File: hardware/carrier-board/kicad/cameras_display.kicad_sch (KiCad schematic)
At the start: 0 parts

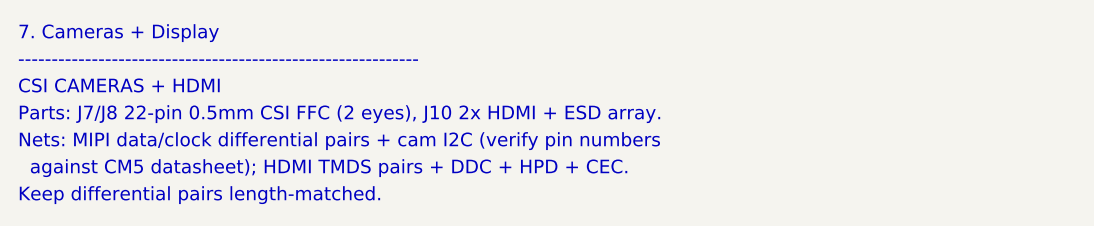
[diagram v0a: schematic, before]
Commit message: Carrier docs + KiCad plan: full two-brain pass (CM5 HUB75 + RP2354B I/O)
Propagate the two-brain architecture across the whole doc set and KiCad plan:
- REQUIREMENTS: restructured M1-M12 (CM5 HUB75; RP2354B core/MAX7219/WS2812/
  sensors/buttons/servos; USB selector + standalone program port); N-list reworked.
- POWER: add +V_SERVO and +3V3_RP rails, servo current budget, updated worked
  total + protection; sensors now on +3V3_RP not CM5 3V3.
- CONNECTORS: J3 re-sourced to RP2354B SPI0, J4 4 WS2812 zones, J5 +SENS_INT,
  J6 BTN1..10, add J12 USB-C, J20-J27 servos, SW1 USB selector, SWD/UART hdrs;
  drop JP1/JP2; fans presented as RP2354B-default-or-CM5 (decision flagged).
- BOM: add RP2354B core, '125/'245 (RP side), USB mux/USB-C/ESD, servo headers,
  +3V3_RP reg; fix '125 double-count and stale HUB75/MAX7219-shared-buffer/JP1.
- MULTI-BACKEND: HUB75+MAX7219 now simultaneous (different brains); firmware
  CompositePanelOutput is the sole remaining blocker.
- IO-EXPANSION: RP2354B is the primary I/O backbone; I2C expanders secondary.
- kicad: 11-sheet plan, stable UUIDs, generator skips populated face_buffer.
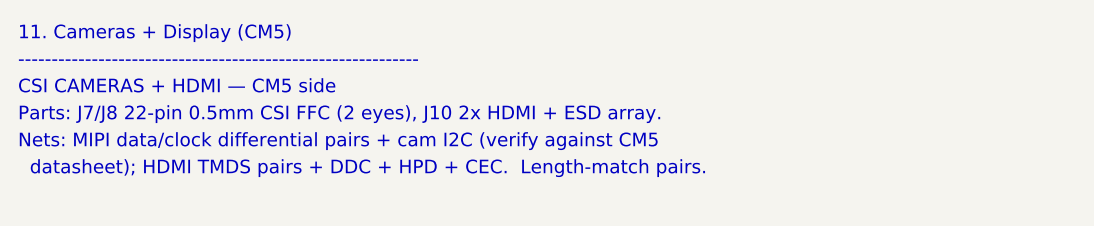
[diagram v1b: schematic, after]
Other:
- note added: "11. Cameras + Display (CM5)"
- note added: "CSI CAMERAS + HDMI — CM5 side"
- note added: "Nets: MIPI data/clock differential pairs + cam I2C (verify against CM5"
- note added: "datasheet); HDMI TMDS pairs + DDC + HPD + CEC. Length-match pairs."
- note removed: "7. Cameras + Display"
- note removed: "CSI CAMERAS + HDMI"
- note removed: "Keep differential pairs length-matched."
- note removed: "Nets: MIPI data/clock differential pairs + cam I2C (verify pin numbers"
- note removed: "against CM5 datasheet); HDMI TMDS pairs + DDC + HPD + CEC."
- title: ProtoHUD Carrier — 7. Cameras + Display -> ProtoHUD Carrier — 11. Cameras + Display (CM5)
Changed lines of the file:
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@@
   (paper "A3")
   (title_block
-    (title "ProtoHUD Carrier — 7. Cameras + Display")
+    (title "ProtoHUD Carrier — 11. Cameras + Display (CM5)")
     (rev "A")
     (company "ProtoHUD")
   )
-  (text "7. Cameras + Display" (at 25.4 25.40 0) (effects (font (size 1.5 1.5)) (justify left bottom)))
+  (text "11. Cameras + Display (CM5)" (at 25.4 25.40 0) (effects (font (size 1.5 1.5)) (justify left bottom)))
   (text "------------------------------------------------------------" (at 25.4 28.40 0) (effects (font (size 1.5 1.5)) (justify left bottom)))
-  (text "CSI CAMERAS + HDMI" (at 25.4 31.40 0) (effects (font (size 1.5 1.5)) (justify left bottom)))
+  (text "CSI CAMERAS + HDMI — CM5 side" (at 25.4 31.40 0) (effects (font (size 1.5 1.5)) (justify left bottom)))
   (text "Parts: J7/J8 22-pin 0.5mm CSI FFC (2 eyes), J10 2x HDMI + ESD array." (at 25.4 34.40 0) (effects (font (size 1.5 1.5)) (justify left bottom)))
-  (text "Nets: MIPI data/clock differential pairs + cam I2C (verify pin numbers" (at 25.4 37.40 0) (effects (font (size 1.5 1.5)) (justify left bottom)))
-  (text "  against CM5 datasheet); HDMI TMDS pairs + DDC + HPD + CEC." (at 25.4 40.40 0) (effects (font (size 1.5 1.5)) (justify left bottom)))
-  (text "Keep differential pairs length-matched." (at 25.4 43.40 0) (effects (font (size 1.5 1.5)) (justify left bottom)))
+  (text "Nets: MIPI data/clock differential pairs + cam I2C (verify against CM5" (at 25.4 37.40 0) (effects (font (size 1.5 1.5)) (justify left bottom)))
+  (text "  datasheet); HDMI TMDS pairs + DDC + HPD + CEC.  Length-match pairs." (at 25.4 40.40 0) (effects (font (size 1.5 1.5)) (justify left bottom)))
   (sheet_instances
     (path "/" (page "1"))

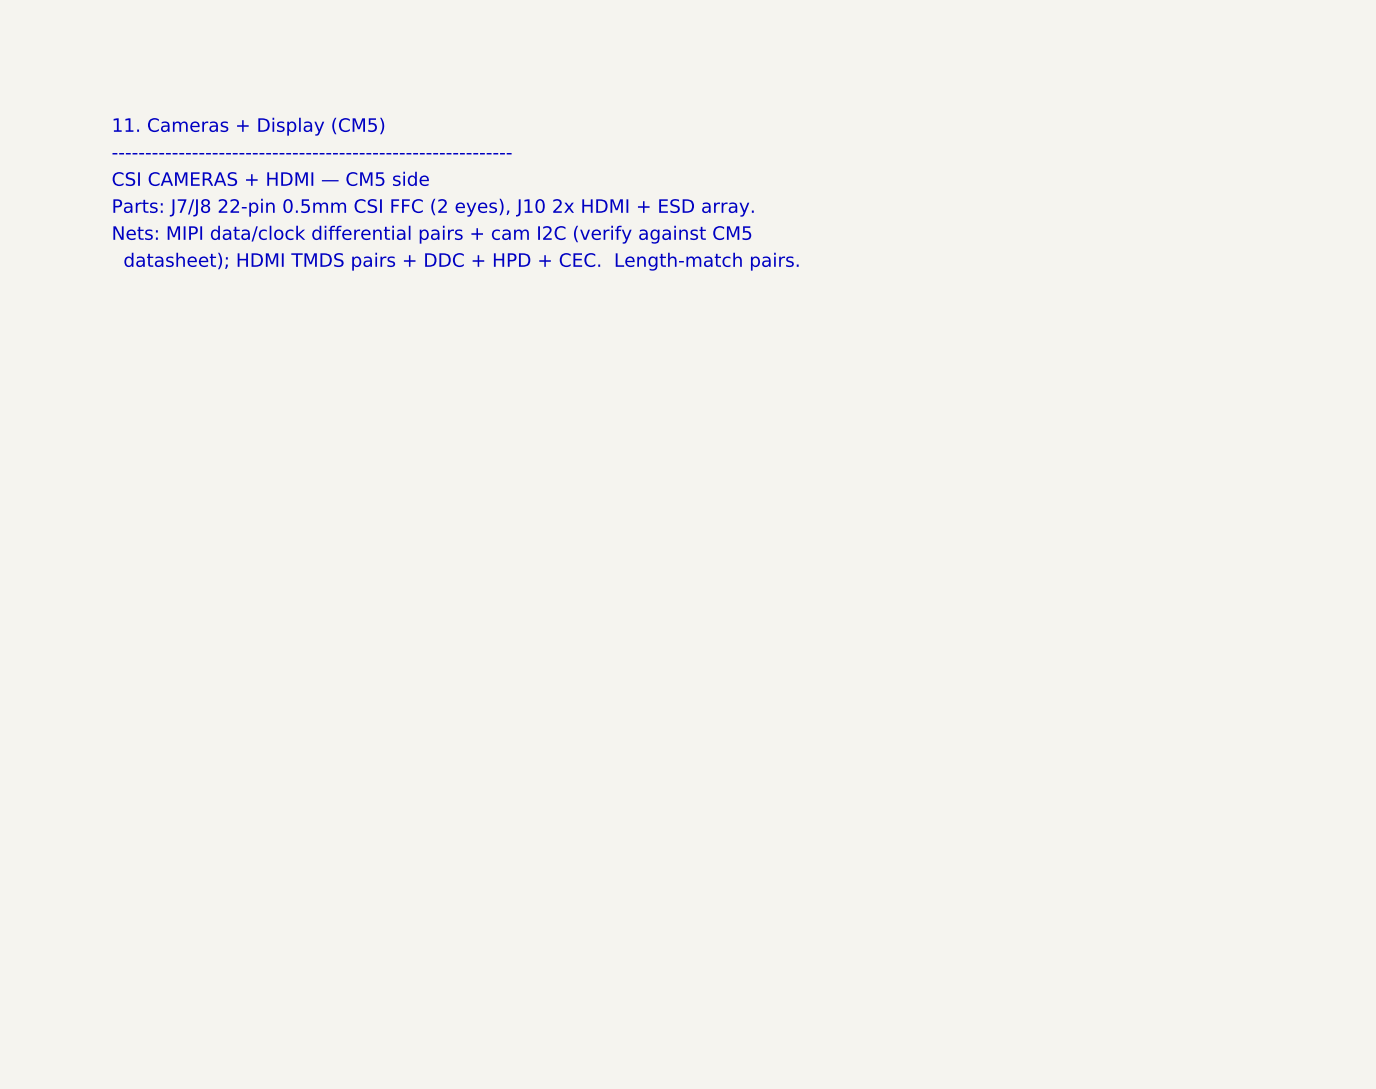
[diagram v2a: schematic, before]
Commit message: Carrier KiCad: populate all 11 schematic sheets
Replace populate_face_buffer.py with populate_sheets.py: one generator that
emits all 11 populated sub-sheets reusing the KiCad-9 format proven by the
face_buffer proof. Shared symbol library + generic box-symbol builder; condensed
CM5 (2x DF40-100) and RP2354B (QFN-80) symbols showing only used pins.

Connectivity by net labels (global for rails + cross-sheet nets: GPIOxx HUB75,
MX_*, LED*_DAT, SRV*, BTN*, *_USB_*; local within-sheet). Sheets: power
(protection + rails + AP2112 +3V3_RP), cm5 (HUB75 out + fan MOSFETs + RP ctrl),
face_buffer, rp2354_io (RP2354B + xtal + SW1/J12 + ESD + SWD), rp2354_face
(U10->J3), leds (U11 quad ->J4a-d), sensors_i2c (pull-ups+J5+STEMMA),
servos (J20-27 + rail), gpio_buttons (J6), usb (USB2514B hub + uplink),
cameras_display (CSI FFC + HDMI).

Verified: all sheets paren-balanced, every used lib_id defined, all instance
paths match sheet UUIDs, root<->sub-sheet UUID linkage intact. generate_skeleton.py
now lists all sheets POPULATED (writes only root+project). Not yet opened in
KiCad here -- expect ERC warnings (PWR_FLAG, unconnected pins) to clean.
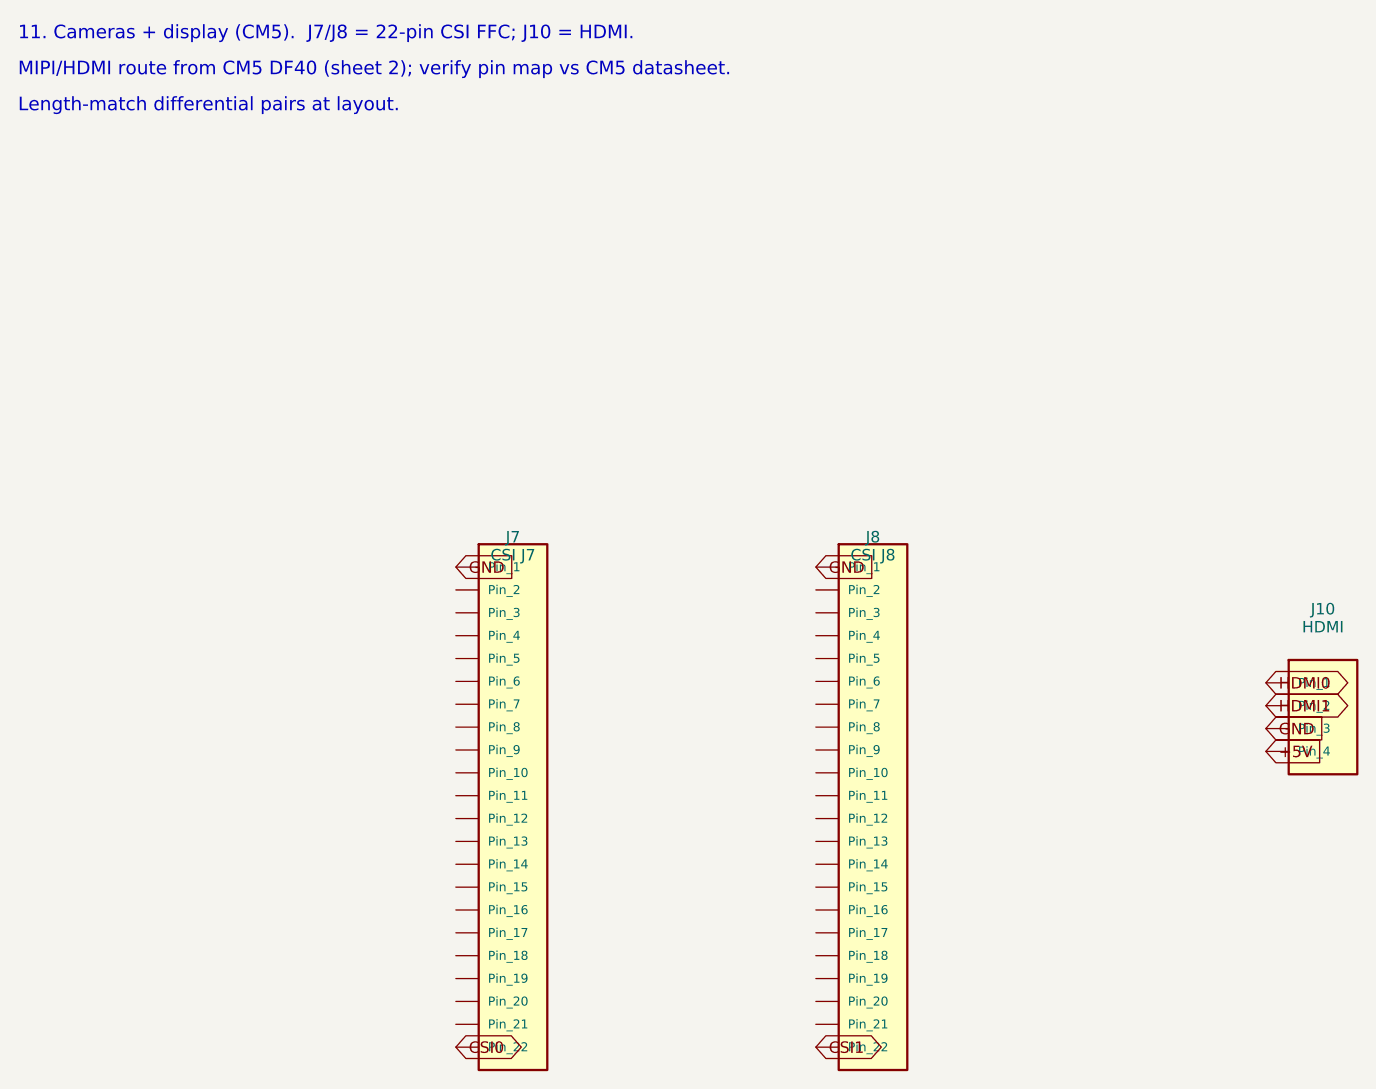
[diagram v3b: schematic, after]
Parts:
- added J10: HDMI, symbol Connector_Generic:Conn_01x04
- added J7: CSI J7, symbol Connector_Generic:Conn_01x22
- added J8: CSI J8, symbol Connector_Generic:Conn_01x22
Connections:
- new net +5V: J10.4 (Pin_4)
- new net CSI0: J7.22 (Pin_22)
- new net CSI1: J8.22 (Pin_22)
- new net GND: J10.3 (Pin_3), J7.1 (Pin_1), J8.1 (Pin_1)
- new net HDMI0: J10.1 (Pin_1)
- new net HDMI1: J10.2 (Pin_2)
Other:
- note added: "11. Cameras + display (CM5). J7/J8 = 22-pin CSI FFC; J10 = HDMI."
- note added: "Length-match differential pairs at layout."
- note added: "MIPI/HDMI route from CM5 DF40 (sheet 2); verify pin map vs CM5 datasheet."
- note removed: "------------------------------------------------------------"
- note removed: "11. Cameras + Display (CM5)"
- note removed: "CSI CAMERAS + HDMI — CM5 side"
- note removed: "Nets: MIPI data/clock differential pairs + cam I2C (verify against CM5"
- note removed: "Parts: J7/J8 22-pin 0.5mm CSI FFC (2 eyes), J10 2x HDMI + ESD array."
- note removed: "datasheet); HDMI TMDS pairs + DDC + HPD + CEC. Length-match pairs."
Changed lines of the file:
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@@
 (kicad_sch
-  (version 20230121)
-  (generator protohud_skeleton)
+  (version 20250114)
+  (generator "protohud_populate")
+  (generator_version "9.0")
   (paper "A3")
   (title_block
@@
     (company "ProtoHUD")
   )
-  (text "11. Cameras + Display (CM5)" (at 25.4 25.40 0) (effects (font (size 1.5 1.5)) (justify left bottom)))
-  (text "------------------------------------------------------------" (at 25.4 28.40 0) (effects (font (size 1.5 1.5)) (justify left bottom)))
-  (text "CSI CAMERAS + HDMI — CM5 side" (at 25.4 31.40 0) (effects (font (size 1.5 1.5)) (justify left bottom)))
-  (text "Parts: J7/J8 22-pin 0.5mm CSI FFC (2 eyes), J10 2x HDMI + ESD array." (at 25.4 34.40 0) (effects (font (size 1.5 1.5)) (justify left bottom)))
-  (text "Nets: MIPI data/clock differential pairs + cam I2C (verify against CM5" (at 25.4 37.40 0) (effects (font (size 1.5 1.5)) (justify left bottom)))
-  (text "  datasheet); HDMI TMDS pairs + DDC + HPD + CEC.  Length-match pairs." (at 25.4 40.40 0) (effects (font (size 1.5 1.5)) (justify left bottom)))
+  (text "11. Cameras + display (CM5).  J7/J8 = 22-pin CSI FFC; J10 = HDMI." (at 15 15.0 0) (effects (font (size 1.5 1.5)) (justify left bottom)))
+  (text "MIPI/HDMI route from CM5 DF40 (sheet 2); verify pin map vs CM5 datasheet." (at 15 19.0 0) (effects (font (size 1.5 1.5)) (justify left bottom)))
+  (text "Length-match differential pairs at layout." (at 15 23.0 0) (effects (font (size 1.5 1.5)) (justify left bottom)))
+  (symbol
+    (lib_id "Connector_Generic:Conn_01x22")
+    (at 70.00 100.00 0)
+    (unit 1)
+    (exclude_from_sim no) (in_bom yes) (on_board yes) (dnp no)
+    (property "Reference" "J7" (at 70.00 70.00 0) (effects (font (size 1.27 1.27))))
+    (property "Value" "CSI J7" (at 70.00 72.00 0) (effects (font (size 1.27 1.27))))
+    (property "Footprint" "" (at 70.00 100.00 0) (effects (font (size 1.27 1.27)) (hide yes)))
+    (property "Datasheet" "" (at 70.00 100.00 0) (effects (font (size 1.27 1.27)) (hide yes)))
+    (pin "1")
+    (pin "2")
+    (pin "3")
+    (pin "4")
+    (pin "5")
+    (pin "6")
+    (pin "7")
+    (pin "8")
+    (pin "9")
+    (pin "10")
+    (pin "11")
+    (pin "12")
+    (pin "13")
+    (pin "14")
+    (pin "15")
+    (pin "16")
+    (pin "17")
+    (pin "18")
+    (pin "19")
+    (pin "20")
+    (pin "21")
+    (pin "22")
+    (instances
+      (project "ProtoHUD-Carrier"
+        (path "/c814e905-b80c-42d1-beeb-925e48192849"
+          (reference "J7") (unit 1))))
+  )
+  (symbol
+    (lib_id "Connector_Generic:Conn_01x22")
+    (at 110.00 100.00 0)
+    (unit 1)
+    (exclude_from_sim no) (in_bom yes) (on_board yes) (dnp no)
+    (property "Reference" "J8" (at 110.00 70.00 0) (effects (font (size 1.27 1.27))))
+    (property "Value" "CSI J8" (at 110.00 72.00 0) (effects (font (size 1.27 1.27))))
+    (property "Footprint" "" (at 110.00 100.00 0) (effects (font (size 1.27 1.27)) (hide yes)))
+    (property "Datasheet" "" (at 110.00 100.00 0) (effects (font (size 1.27 1.27)) (hide yes)))
+    (pin "1")
+    (pin "2")
+    (pin "3")
+    (pin "4")
+    (pin "5")
+    (pin "6")
+    (pin "7")
+    (pin "8")
+    (pin "9")
+    (pin "10")
+    (pin "11")
+    (pin "12")
+    (pin "13")
+    (pin "14")
+    (pin "15")
+    (pin "16")
+    (pin "17")
+    (pin "18")
+    (pin "19")
+    (pin "20")
+    (pin "21")
+    (pin "22")
+    (instances
+      (project "ProtoHUD-Carrier"
+        (path "/c814e905-b80c-42d1-beeb-925e48192849"
+          (reference "J8") (unit 1))))
+  )
+  (symbol
+    (lib_id "Connector_Generic:Conn_01x04")
+    (at 160.00 90.00 0)
+    (unit 1)
+    (exclude_from_sim no) (in_bom yes) (on_board yes) (dnp no)
+    (property "Reference" "J10" (at 160.00 78.00 0) (effects (font (size 1.27 1.27))))
+    (property "Value" "HDMI" (at 160.00 80.00 0) (effects (font (size 1.27 1.27))))
+    (property "Footprint" "" (at 160.00 90.00 0) (effects (font (size 1.27 1.27)) (hide yes)))
+    (property "Datasheet" "" (at 160.00 90.00 0) (effects (font (size 1.27 1.27)) (hide yes)))
+    (pin "1")
+    (pin "2")
+    (pin "3")
+    (pin "4")
+    (instances
+      (project "ProtoHUD-Carrier"
+        (path "/c814e905-b80c-42d1-beeb-925e48192849"
+          (reference "J10") (unit 1))))
+  )
+  (global_label "GND" (shape input) (at 63.65 73.33 180) (effects (font (size 1.27 1.27)) (justify left)))
+  (global_label "CSI0" (shape bidirectional) (at 63.65 126.67 180) (effects (font (size 1.27 1.27)) (justify left)))
+  (global_label "GND" (shape input) (at 103.65 73.33 180) (effects (font (size 1.27 1.27)) (justify left)))
+  (global_label "CSI1" (shape bidirectional) (at 103.65 126.67 180) (effects (font (size 1.27 1.27)) (justify left)))
+  (global_label "HDMI0" (shape bidirectional) (at 153.65 86.19 180) (effects (font (size 1.27 1.27)) (justify left)))
+  (global_label "HDMI1" (shape bidirectional) (at 153.65 88.73 180) (effects (font (size 1.27 1.27)) (justify left)))
+  (global_label "GND" (shape input) (at 153.65 91.27 180) (effects (font (size 1.27 1.27)) (justify left)))
+  (global_label "+5V" (shape input) (at 153.65 93.81 180) (effects (font (size 1.27 1.27)) (justify left)))
   (sheet_instances
     (path "/" (page "1"))
